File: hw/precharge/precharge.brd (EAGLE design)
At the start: 36 x 25 mm, 32 parts, among them Q1 TPH1R204PL, Q2 TPH1R204PL, U1 ZXTR2012Z, U2 LP2985SOT-23-5, U3 ATTINY44A-SSU, U4 MIC4416, U5 MIC4416

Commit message: Continued iteration on precharge board
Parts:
- added R8, R9: 100k 1%, mfpassives:R0603
- moved JP1 0.60 mm to (16.0, 5.90)
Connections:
- net FET_MAIN: now also R9.P$2
- net FET_PRECHARGE: now also R8.P$2
- net GND: now also R8.P$1, R9.P$1
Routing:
- net FET_PRECHARGE: track 14.7 -> 19.8 mm
- net GND: track 15.7 -> 19.5 mm
- net FET_MAIN: track 17.1 -> 19.9 mm, vias 2 -> 3
- net RST: track 10.4 -> 7.69 mm
- net SCK: track 4.96 -> 5.56 mm
- net MISO: track 3.39 -> 3.99 mm

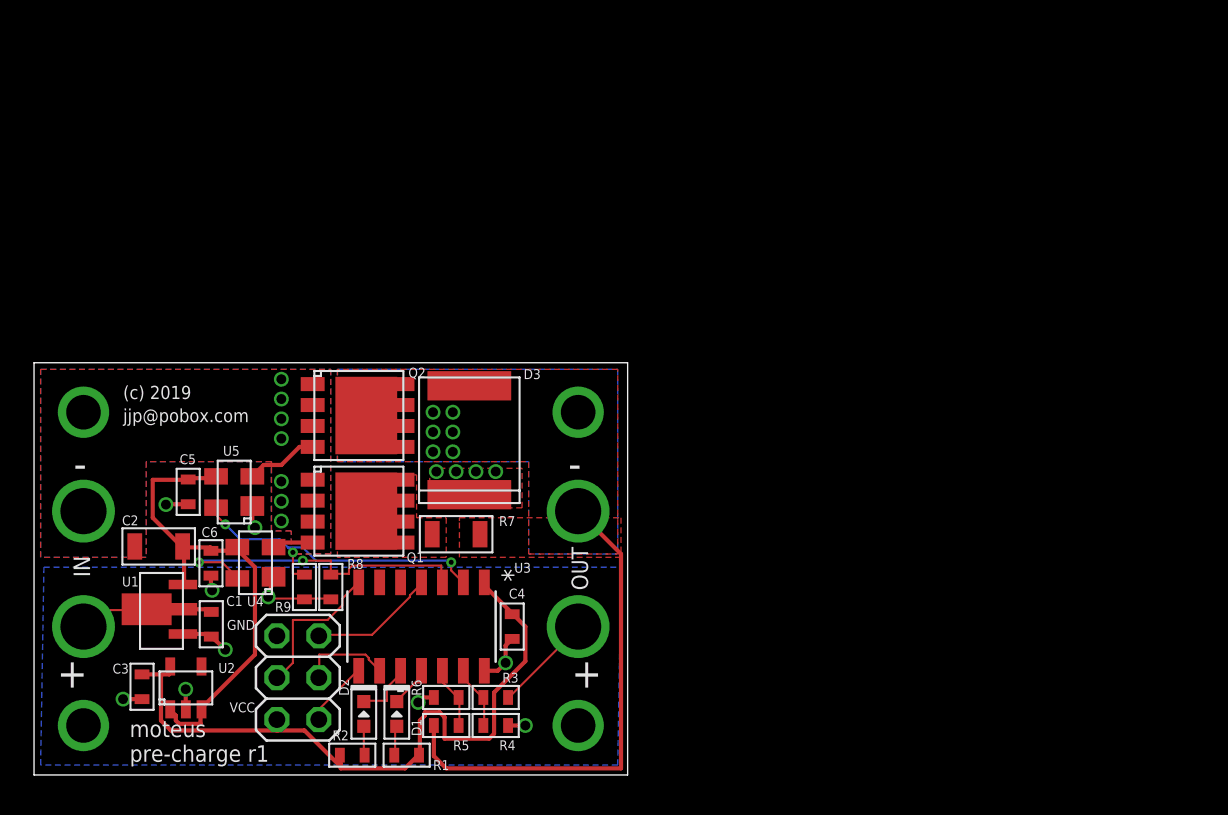
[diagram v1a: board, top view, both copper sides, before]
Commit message: Updated pre-charge, now named "power distribution"
Nominally everything but auto-route
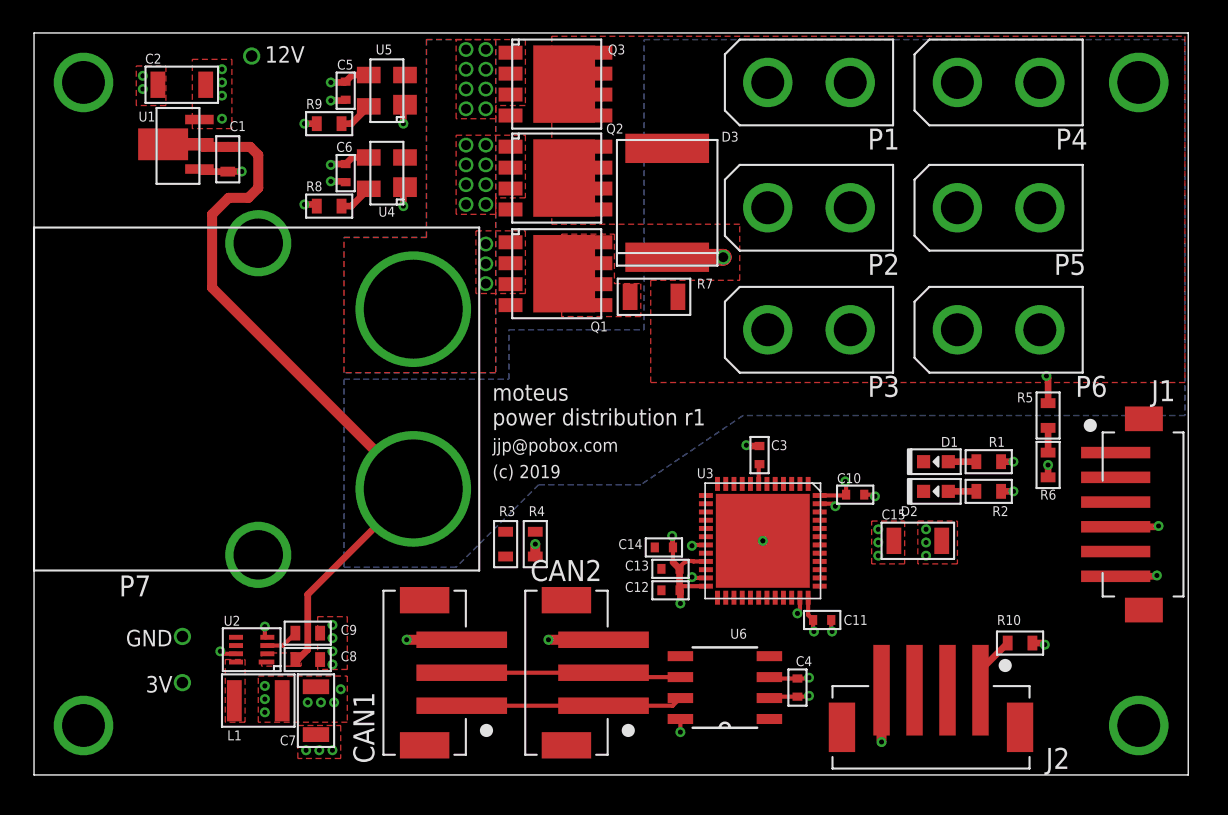
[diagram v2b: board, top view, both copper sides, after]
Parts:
- removed JP1: (no value), pinhead:2X03
- removed V+, V+OUT, V-, V-OUT: PAD12AWG_PAD, controller:12AWG_PAD
- added C10, C11, C12, C13: 0.1uF, mfpassives:C0402
- added C14: 1uF, mfpassives:C0402
- added C15, C7: 10uF 35V, mfpassives:C1206
- added C8, C9: 1uF 50V, mfpassives:C0603
- added CAN1, CAN2: JST-PH3SMT_VERT, precharge:JST_B3B_PH-SM4-TB(LF)(SN)
- added D12, D3V3, DG: PAD24AWG_PAD, precharge:24AWG_PAD
- added J1: JST-ZH6SMT_VERT, precharge:JST_B6B-ZR-SM4-TF(LF)(SN)
- added J2: JST-PH4SMT_VERT, precharge:JST_B4B_PH-SM4-TB(LF)(SN)
- added L1: 33uH, mfpassives:L1210
- added P1, P2, P3, P4, P5, P6: XT30P, precharge:XT30P
- added P7: XT90PW-M, precharge:XT90PW-M
- added Q3: TPH1R204PL, imu_junction:SOP_ADVANCE
- added R10: 220, mfpassives:R0603
- added U6: TCAN334G, precharge:SOT23-8
- C3: value 2.2uF -> 0.1uF; device mfpassives:C0603 -> mfpassives:C0402
- C4, C5, C6: device mfpassives:C0603 -> mfpassives:C0402
- U$1, U$2, U$3, U$4: value MOUNTM2 -> MOUNT; device controller:M2MOUNT -> precharge:M2.5MOUNT
- U2: value LP2985SOT-23-5 -> MAX150628TDFN; device precharge:SOT-23-5 -> precharge:8TDFN
- U3: value ATTINY44A-SSU -> STM32G474CEU6; device absolute_position:14S1 -> precharge:QFN50P700X700X60-49N
- moved R2 41.8 mm to (57.9, 17.2), turned to 0 degrees
- moved R5 41.1 mm to (61.5, 21.8), turned to 90 degrees
- moved C3 40.0 mm to (44.0, 19.4), turned to 90 degrees
- moved R1 39.5 mm to (57.9, 19.0)
- moved U$1 39.4 mm to (67.0, 42.0)
- moved R6 39.1 mm to (61.5, 18.8), turned to 90 degrees
- moved D2 37.2 mm to (54.7, 17.2), turned to 0 degrees
- moved D1 36.1 mm to (54.7, 19.0), turned to 0 degrees
- moved U$4 34.0 mm to (67.0, 3.00)
- moved C1 28.2 mm to (11.8, 37.3)
- moved U1 28.2 mm to (8.83, 38.2)
- moved R9 28.1 mm to (17.9, 39.5), turned to 0 degrees
- moved C2 28.0 mm to (8.96, 41.9)
- moved C5 26.1 mm to (18.9, 41.5)
- moved U5 26.0 mm to (21.4, 41.5)
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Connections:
- removed net MISO: JP1.1, U3.8
- removed net MOSI: JP1.4, U3.7
- removed net N$5: D2.CATHODE, U3.10
- removed net RST: JP1.5, U3.4
- removed net SCK: JP1.3, U3.9
- new net CAN_N: CAN1.2, CAN2.2, U6.6
- new net CAN_P: CAN1.1, CAN2.1, U6.7
- new net CAN_RX: U3.33, U6.4
- new net CAN_SHDN: U3.32, U6.5
- new net CAN_TX: U3.34, U6.1
- new net LED1: D1.CATHODE, U3.4
- new net LED2: D2.CATHODE, U3.3
- new net LX: L1.P$1, U2.8
- new net N$13: C9.P$1, U2.3
- new net NRST: C3.P$1, J1.2, U3.7
- new net PWR_LED: J2.2, U3.10
- new net PWR_SW: J2.3, U3.11
- new net SWCLK: J1.5, U3.38
- new net SWDIO: J1.3, U3.37
- net +12V: now also D12.P$1; no longer U2.1, U2.3
- net +18V: now also C8.P$1, P1.2, P2.2, P3.2, P4.2, P5.2, P6.2, P7.1, U2.1, U2.2; no longer V+.1, V+OUT.1
- net FET_MAIN: now also U3.9; no longer U3.2
- net FET_PRECHARGE: now also U3.8; no longer U3.3
- net GND: now also C10.P$2, C11.P$2, C12.P$2, C13.P$2, C14.P$2, C15.P$2, C7.P$2, C8.P$2, C9.P$2, CAN1.3, CAN2.3, DG.P$1, J1.4, J2.4, P7.2, Q3.1, Q3.2, Q3.3, U2.7, U3.19, U3.23, U3.35, U3.47, U3.49, U6.2, U6.8; no longer JP1.6, U2.2, U3.14, V-.1
- net N$2: now also J2.1, R10.P$1; no longer D1.CATHODE, U3.11
- net N$3: now also Q3.4
- net V-OUT: now also P1.1, P2.1, P3.1, P4.1, P5.1, P6.1, Q3.5, Q3.6, Q3.7, Q3.8, Q3.PAD; no longer V-OUT.1
- net VCC: now also C10.P$1, C11.P$1, C12.P$1, C13.P$1, C14.P$1, C15.P$1, C7.P$1, D3V3.P$1, J1.6, L1.P$2, R10.P$2, U2.4, U3.20, U3.21, U3.24, U3.36, U3.48, U6.3; no longer C3.P$1, JP1.2, U2.5, U3.1
- net VSAMP_IN: now also U3.31; no longer U3.13
- net VSAMP_OUT: now also U3.30; no longer U3.12
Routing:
- net +18V: track 15.0 -> 50.0 mm, vias 4 -> 1
- net V-OUT: track 30.2 -> 1.69 mm, vias 6 -> 1
- net +12V: track 29.8 -> 4.97 mm, vias 0 -> 6
- net VCC: track 43.6 -> 21.2 mm, vias 0 -> 20
- net FET_MAIN: track 19.9 -> 2.08 mm, vias 3 -> 0
- net FET_PRECHARGE: track 19.8 -> 2.08 mm, vias 2 -> 0
- net CAN_P: track 0.00 -> 13.5 mm
- net CAN_N: track 0.00 -> 13.4 mm
- net GND: track 19.5 -> 32.8 mm, vias 17 -> 55
- net MOSI: track 9.11 -> 0.00 mm
- net RST: track 7.69 -> 0.00 mm
- net SCK: track 5.56 -> 0.00 mm
- net N$3: track 4.40 -> 0.00 mm
- net MISO: track 3.99 -> 0.00 mm
- net VSAMP_IN: track 3.97 -> 0.00 mm
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- added copper zone on layer 1, net +12V
- added copper zone on layer 15, net +12V
- added copper zone on layer 1, net LX
- added copper zone on layer 1, net VCC
- added copper zone on layer 15, net VCC
- removed copper zone on layer 15, net V-OUT
- removed copper zone on layer 16, net V-OUT
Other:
- board size 36 x 25 mm -> 70 x 45 mm
- board text added: "12V"
- board text added: "3V"
- board text added: "moteus power distribution r1"
- board text removed: "+"
- board text removed: "-"
- board text removed: "IN"
- board text removed: "OUT"
- board text removed: "VCC"
- board text removed: "moteus pre-charge r1"

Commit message: power_dist: All BOM filled in
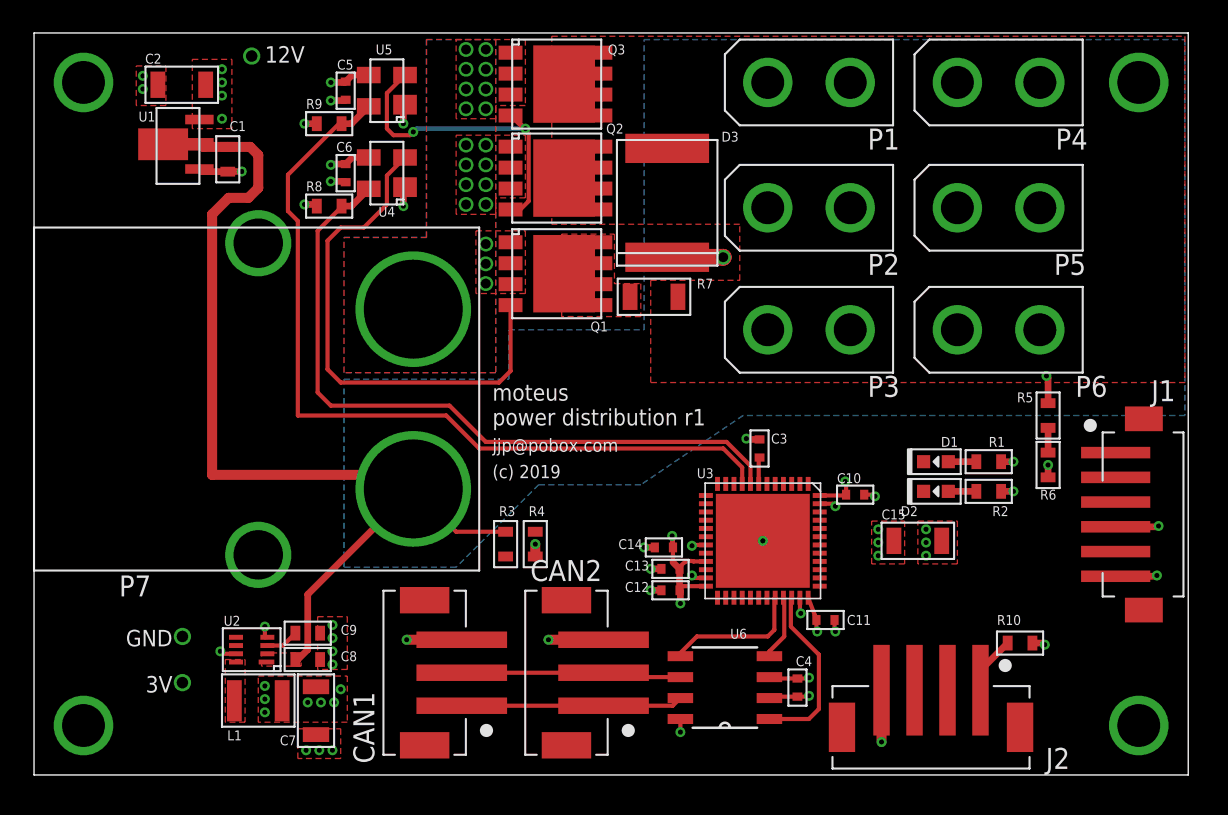
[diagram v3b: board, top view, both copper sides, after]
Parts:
- moved C3 0.40 mm to (44.0, 19.8)
- moved C11 0.20 mm to (48.0, 9.40)
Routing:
- net FET_MAIN: track 2.08 -> 50.7 mm
- net FET_PRECHARGE: track 2.08 -> 43.2 mm
- net N$12: track 0.00 -> 31.3 mm
- net N$3: track 0.00 -> 20.6 mm, vias 0 -> 2
- net +18V: track 50.0 -> 63.8 mm
- net CAN_TX: track 0.00 -> 10.7 mm
- net CAN_SHDN: track 0.00 -> 8.45 mm
- net CAN_RX: track 0.00 -> 3.94 mm
- net GND: track 32.8 -> 34.8 mm, vias 55 -> 58

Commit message: power dist: Fix some silks and MPNs found by macrofab
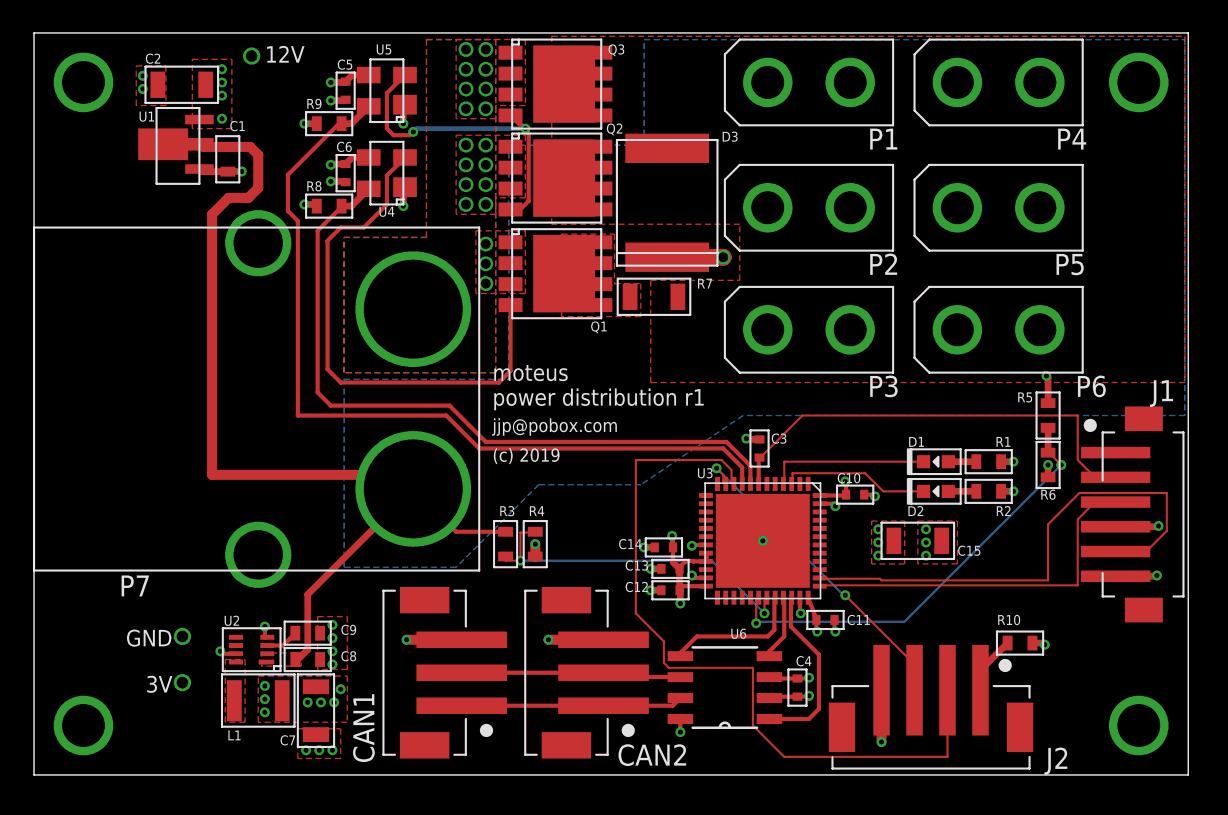
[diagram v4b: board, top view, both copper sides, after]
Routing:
- net PWR_LED: track 0.00 -> 45.6 mm
- net SWCLK: track 0.00 -> 31.2 mm
- net NRST: track 1.62 -> 27.4 mm
- net VSAMP_OUT: track 1.50 -> 26.7 mm, vias 0 -> 2
- net SWDIO: track 0.00 -> 22.4 mm
- net VSAMP_IN: track 0.00 -> 20.9 mm, vias 0 -> 2
- net PWR_SW: track 0.00 -> 19.7 mm, vias 0 -> 2
- net LED1: track 0.00 -> 9.82 mm
- net LED2: track 0.00 -> 9.08 mm
- net VCC: track 21.2 -> 21.8 mm

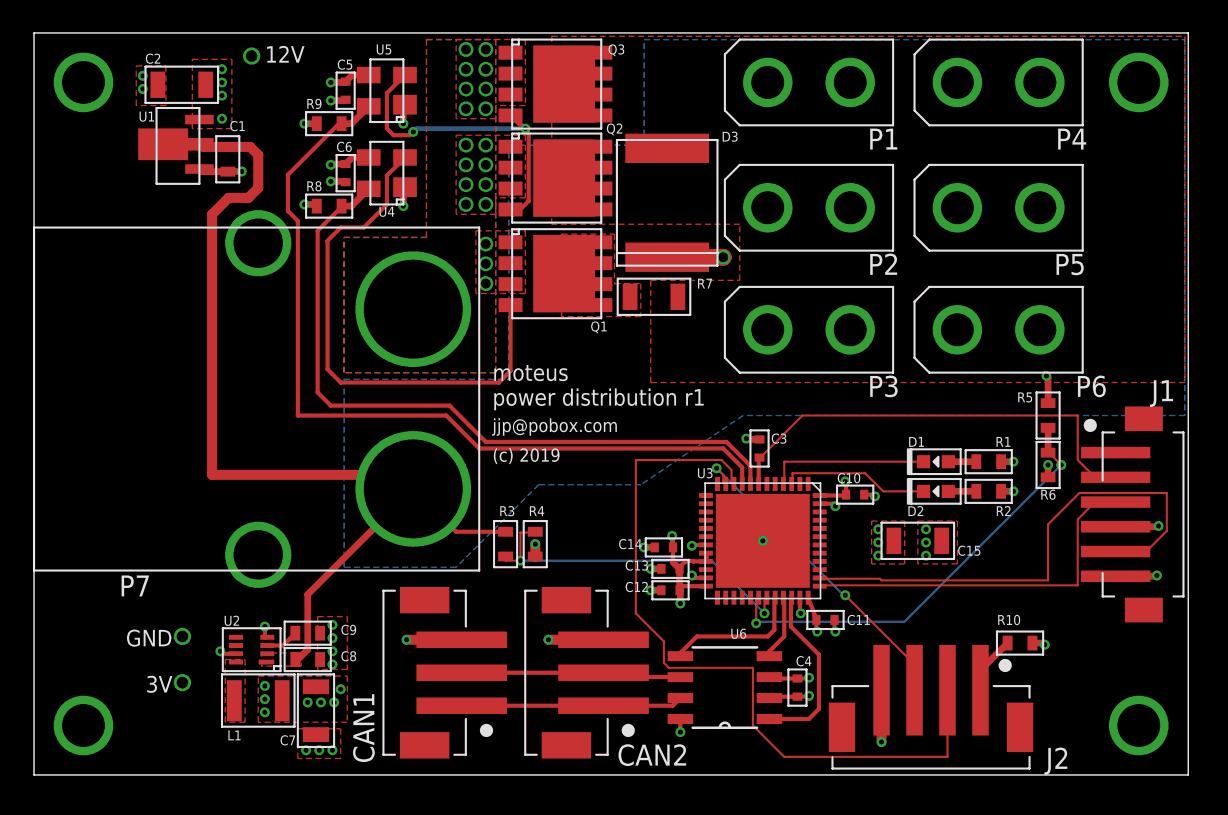
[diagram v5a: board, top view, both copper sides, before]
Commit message: Update power dist board to r2
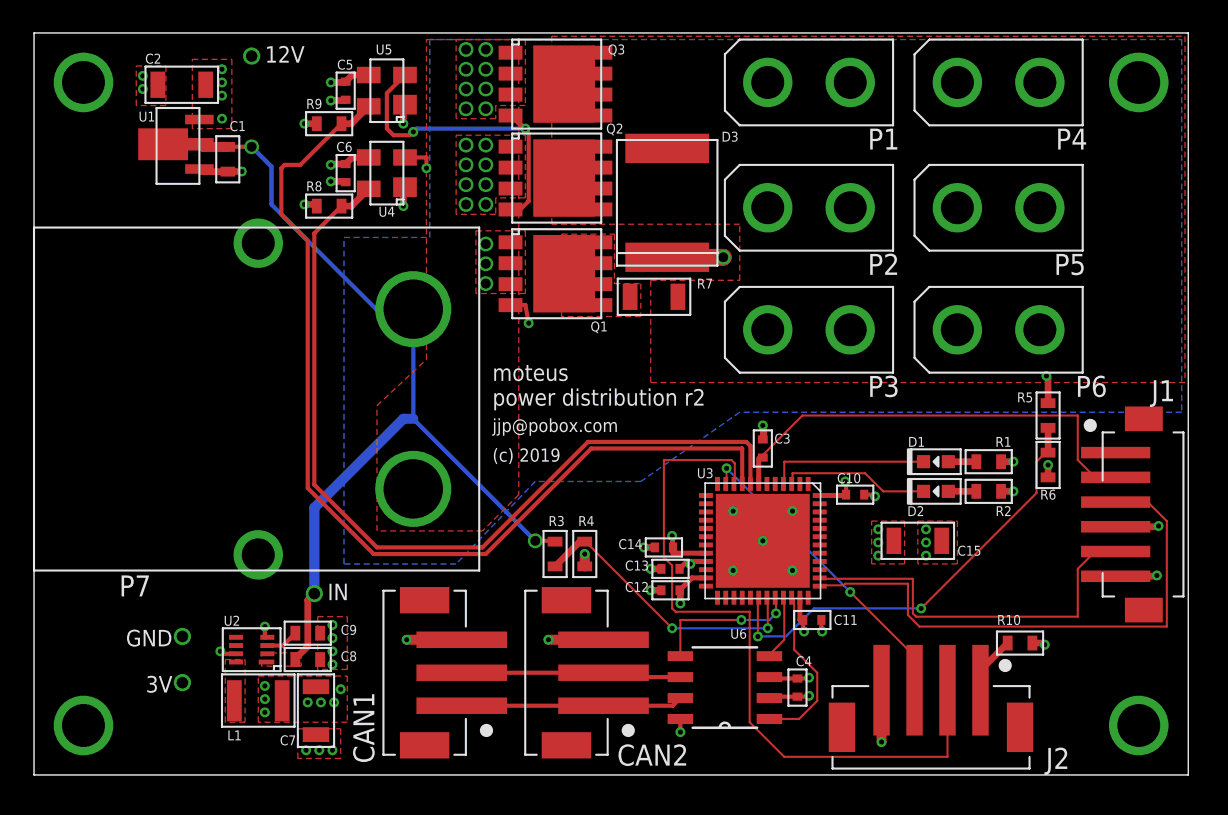
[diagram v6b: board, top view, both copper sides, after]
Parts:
- added DI: PAD24AWG_PAD, precharge:24AWG_PAD
- moved R3 3.06 mm to (31.6, 13.4)
- moved R4 3.06 mm to (33.4, 13.4)
- moved C11 0.80 mm to (47.2, 9.40)
- moved C3 0.20 mm to (44.2, 19.8)
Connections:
- net +18V: now also DI.P$1, P7.2; no longer P7.1
- net GND: now also P7.1; no longer P7.2, U3.19, U3.23, U3.35, U3.47
- net VCC: now also U3.23, U3.35; no longer U3.24, U3.36
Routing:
- net N$12: track 31.3 -> 18.8 mm, vias 0 -> 2
- net SWDIO: track 22.4 -> 33.3 mm
- net FET_PRECHARGE: track 43.2 -> 52.7 mm
- net FET_MAIN: track 50.7 -> 59.7 mm
- net SWCLK: track 31.2 -> 23.5 mm
- net GND: track 34.8 -> 30.9 mm
- net +18V: track 63.8 -> 60.3 mm, vias 1 -> 3
- net VSAMP_IN: track 20.9 -> 17.6 mm
- net PWR_LED: track 45.6 -> 43.3 mm
- net CAN_SHDN: track 8.45 -> 9.13 mm, vias 0 -> 2
- net PWR_SW: track 19.7 -> 19.2 mm
- net VCC: track 21.8 -> 21.4 mm, vias 20 -> 21
- removed copper zone on layer 15, net GND
- removed copper zone on layer 16, net GND
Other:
- board text added: "IN"
- board text added: "moteus power distribution r2"
- board text removed: "moteus power distribution r1"

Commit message: More power dist errata:
 * Fix 10k resistors
 * Rename TCAN package to actually be SOIC8, since that is what it is
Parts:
- U6: device precharge:SOT23-8 -> precharge:SOIC8
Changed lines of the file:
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@@
 <attribute name="HOUSEPART" value="" x="70.23" y="40.07" size="1.778" layer="27" rot="R90" display="off"/>
 <attribute name="TOLERANCE" value="" x="70.23" y="40.07" size="1.778" layer="27" rot="R90" display="off"/>
-<attribute name="MPN" value="ERT-J1VG103FA" x="70.23" y="40.07" size="1.778" layer="27" rot="R90" display="off"/>
+<attribute name="MPN" value="P10.0KHDKR-ND" x="70.23" y="40.07" size="1.778" layer="27" rot="R90" display="off"/>
 <attribute name="POPULATE" value="1" x="70.23" y="40.07" size="1.778" layer="27" rot="R90" display="off"/>
 <attribute name="VOLTAGE" value="" x="70.23" y="40.07" size="1.778" layer="27" rot="R90" display="off"/>
@@
 <attribute name="HOUSEPART" value="" x="98.33" y="53.09" size="1.778" layer="27" rot="R90" display="off"/>
 <attribute name="TOLERANCE" value="" x="98.33" y="53.09" size="1.778" layer="27" rot="R90" display="off"/>
-<attribute name="MPN" value="ERT-J1VG103FA" x="98.33" y="53.09" size="1.778" layer="27" rot="R90" display="off"/>
+<attribute name="MPN" value="P10.0KHDKR-ND" x="98.33" y="53.09" size="1.778" layer="27" rot="R90" display="off"/>
 <attribute name="POPULATE" value="1" x="98.33" y="53.09" size="1.778" layer="27" rot="R90" display="off"/>
 <attribute name="VOLTAGE" value="" x="98.33" y="53.09" size="1.778" layer="27" rot="R90" display="off"/>
@@
 <attribute name="MF" value="JST" x="67.6" y="15.8" size="1.778" layer="27" rot="R270" display="off"/>
 </element>
-<element name="U6" library="precharge" package="SOT23-8" value="TCAN334G" x="41.9" y="5.3" smashed="yes" rot="R180">
+<element name="U6" library="precharge" package="SOIC8" value="TCAN334G" x="41.9" y="5.3" smashed="yes" rot="R180">
 <attribute name="NAME" x="42.2234" y="8.265" size="0.6" layer="25" ratio="10" rot="SR0"/>
 <attribute name="POPULATE" value="1" x="41.9" y="5.3" size="1.778" layer="27" rot="R180" display="off"/>
